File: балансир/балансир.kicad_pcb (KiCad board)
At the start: 2 copper layers, 0 parts

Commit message: добавлена STM32
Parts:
- added C1: 4.7мкФ, 1210, N_RLC:Конденсатор_SMD_1210, F.Cu at (233.8, 99.5)
- added C10: 4.7мкФ, 1210, N_RLC:Конденсатор_SMD_1210, F.Cu at (227.5, 100.9)
- added C11: 4.7мкФ, 1210, N_RLC:Конденсатор_SMD_1210, F.Cu at (227.4, 96.6)
- added C12: 4.7мкФ, 1210, N_RLC:Конденсатор_SMD_1210, F.Cu at (249.5, 82.7)
- added C13: 4.7мкФ, 1210, N_RLC:Конденсатор_SMD_1210, F.Cu at (255.8, 77.1)
- added C14: 4.7мкФ, 1210, N_RLC:Конденсатор_SMD_1210, F.Cu at (227.5, 105.2)
- added C15: 4.7мкФ, 1210, N_RLC:Конденсатор_SMD_1210, F.Cu at (245.0, 87.0)
- added C16: 4.7мкФ, 1210, N_RLC:Конденсатор_SMD_1210, F.Cu at (232.4, 90.9)
- added C17: 4.7мкФ, 1210, N_RLC:Конденсатор_SMD_1210, F.Cu at (240.0, 95.2)
- added C2: 4.7мкФ, 1210, N_RLC:Конденсатор_SMD_1210, F.Cu at (243.2, 78.4)
- added C3: 4.7мкФ, 1210, N_RLC:Конденсатор_SMD_1210, F.Cu at (251.9, 72.8)
- added C4: 4.7мкФ, 1210, N_RLC:Конденсатор_SMD_1210, F.Cu at (221.2, 104.6)
- added C5: 4.7мкФ, 1210, N_RLC:Конденсатор_SMD_1210, F.Cu at (243.2, 82.7)
- added C6: 4.7мкФ, 1210, N_RLC:Конденсатор_SMD_1210, F.Cu at (249.5, 78.4)
- added C7: 4.7мкФ, 1210, N_RLC:Конденсатор_SMD_1210, F.Cu at (238.7, 90.9)
- added C8: 4.7мкФ, 1210, N_RLC:Конденсатор_SMD_1210, F.Cu at (233.7, 95.2)
- added C9: 4.7мкФ, 1210, N_RLC:Конденсатор_SMD_1210, F.Cu at (258.2, 72.8)
- added DA1: МОП-реле_КР293КП4, MOTOR_DD:DIP8, F.Cu at (199.9, 73.3)
- added DA2: МОП-реле_КР293КП4, MOTOR_DD:DIP8, F.Cu at (199.9, 86.4)
- added DD1: ATmega8A-AU, N_DD:микросхема_ATMEGA-8-161AU, F.Cu at (193.8, 114.0)
- added DD2: 5559ИН10_28(UART-RS485), N_DD:SO-8, F.Cu at (223.1, 98.0)
- added G1: стабилизатор_нерегулируемый_LM2931, N_G:Стабилизатор_корпус_TO-92, F.Cu at (231.9, 87.1)
- added R1: Резистор_0,125Вт, N_RLC:Резистор_SMD_0805_0,125Вт, F.Cu at (232.5, 77.1)
- added R10: Резистор_0,125Вт, N_RLC:Резистор_SMD_0805_0,125Вт, F.Cu at (239.7, 98.6)
- added R11: Резистор_0,125Вт, N_RLC:Резистор_SMD_0805_0,125Вт, F.Cu at (245.9, 93.1)
- added R12: Резистор_0,125Вт, N_RLC:Резистор_SMD_0805_0,125Вт, F.Cu at (251.0, 88.8)
- added R13: 20к, 0805, N_RLC:Резистор_SMD_0805_0,125Вт, F.Cu at (233.4, 105.5)
- added R14: Резистор_0,125Вт, N_RLC:Резистор_SMD_0805_0,125Вт, F.Cu at (259.6, 80.6)
- added R15: Резистор_0,125Вт, N_RLC:Резистор_SMD_0805_0,125Вт, F.Cu at (255.5, 83.2)
- added R16: Резистор_0,125Вт, N_RLC:Резистор_SMD_0805_0,125Вт, F.Cu at (237.5, 102.9)
- added R17: Резистор_0,125Вт, N_RLC:Резистор_SMD_0805_0,125Вт, F.Cu at (255.1, 86.2)
- added R2: Резистор_0,125Вт, N_RLC:Резистор_SMD_0805_0,125Вт, F.Cu at (210.5, 106.3)
- added R3: Резистор_0,125Вт, N_RLC:Резистор_SMD_0805_0,125Вт, F.Cu at (236.6, 77.1)
- added R4: Резистор_0,125Вт, N_RLC:Резистор_SMD_0805_0,125Вт, F.Cu at (214.6, 106.3)
- added R5: Резистор_0,125Вт, N_RLC:Резистор_SMD_0805_0,125Вт, F.Cu at (238.8, 85.8)
- added R6: Резистор_0,125Вт, N_RLC:Резистор_SMD_0805_0,125Вт, F.Cu at (244.7, 90.5)
- added R7: Резистор_0,125Вт, N_RLC:Резистор_SMD_0805_0,125Вт, F.Cu at (255.5, 80.6)
- added R8: Резистор_0,125Вт, N_RLC:Резистор_SMD_0805_0,125Вт, F.Cu at (233.4, 102.9)
- added R9: Резистор_0,125Вт, N_RLC:Резистор_SMD_0805_0,125Вт, F.Cu at (251.0, 86.2)
- added VD1: Диод_шоттки(2-анод), N_VD_HL:Диод_BAR43CFILM_SOT-23, F.Cu at (244.5, 99.1)
- added VD10: Диод_шоттки(2-анод), N_VD_HL:Диод_BAR43CFILM_SOT-23, F.Cu at (260.2, 83.6)
- added VD2: Диод_шоттки(2-анод), N_VD_HL:Диод_BAR43CFILM_SOT-23, F.Cu at (255.7, 89.2)
- added VD3: Диод_шоттки(2-анод), N_VD_HL:Диод_BAR43CFILM_SOT-23, F.Cu at (242.3, 102.6)
- added VD4: Диод_шоттки(2-анод), N_VD_HL:Диод_BAR43CFILM_SOT-23, F.Cu at (250.7, 95.4)
- added VD5: Диод_шоттки(2-анод), N_VD_HL:Диод_BAR43CFILM_SOT-23, F.Cu at (247.9, 98.9)
- added VD6: Диод_шоттки(2-анод), N_VD_HL:Диод_BAR43CFILM_SOT-23, F.Cu at (259.8, 87.2)
- added VD7: Диод_шоттки(2-анод), N_VD_HL:Диод_BAR43CFILM_SOT-23, F.Cu at (254.1, 92.8)
- added VD8: Диод_шоттки(2-анод), N_VD_HL:Диод_BAR43CFILM_SOT-23, F.Cu at (250.7, 91.8)
- added VD9: Диод_шоттки(2-анод), N_VD_HL:Диод_BAR43CFILM_SOT-23, F.Cu at (245.7, 102.6)
- added VT1: Транзистор_полевой_P-канал, N_VD_HL:Транзистор_P_IRF9Z24NPBF, F.Cu at (105.5, 87.2)
- added VT2: Транзистор_полевой_P-канал, N_VD_HL:Транзистор_P_IRF9Z24NPBF, F.Cu at (123.0, 87.2)
- added VT3: Транзистор_полевой_P-канал, N_VD_HL:Транзистор_P_IRF9Z24NPBF, F.Cu at (112.8, 62.2)
- added VT4: Транзистор_полевой_P-канал, N_VD_HL:Транзистор_P_IRF9Z24NPBF, F.Cu at (127.0, 63.0)
- added VT5: Транзистор_полевой_P-канал, N_VD_HL:Транзистор_P_IRF9Z24NPBF, F.Cu at (108.4, 143.9)
- added VT6: Транзистор_полевой_P-канал, N_VD_HL:Транзистор_P_IRF9Z24NPBF, F.Cu at (108.4, 149.1)
- added VT7: Транзистор_полевой_N-канал, N_VD_HL:Транзистор_N_STP10NK60Z, F.Cu at (119.2, 143.3)
- added VT8: Транзистор_полевой_N-канал, N_VD_HL:Транзистор_N_STP10NK60Z, F.Cu at (119.2, 148.1)
- added X1: Клеммник_х2, N_X:Клеммник_х2_шаг5, F.Cu at (187.5, 53.5)
- added X2: Клеммник_х2, N_X:Клеммник_х2_шаг5, F.Cu at (202.5, 51.2)
- added X3: Клеммник_х2, N_X:Клеммник_х2_шаг5, F.Cu at (201.4, 101.4)
- added X5: Средняя точка(M12), N_X:Отверстие_М12, F.Cu at (75.0, 84.5)
- added X6: Минус(M12), N_X:Отверстие_М12, F.Cu at (155.0, 84.5)
- added XP1: Вилка_PLD6_ПРОГ, N_X:Вилка_PLD6_вертикальная, F.Cu at (243.8, 74.7)
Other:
- board outline added: 80 x 60 mm

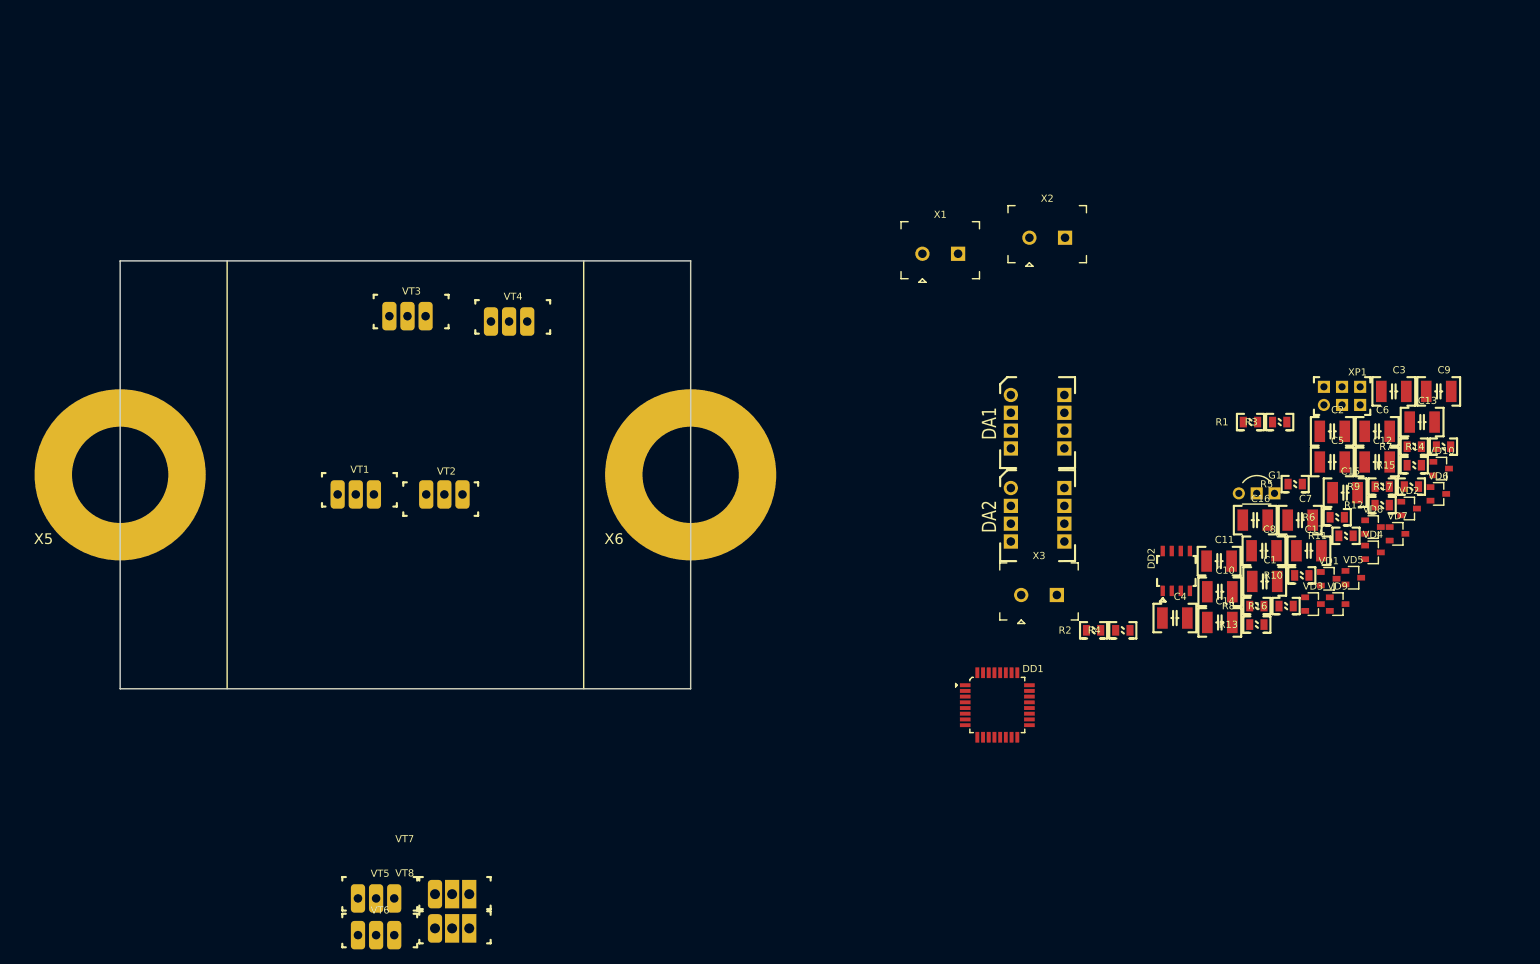
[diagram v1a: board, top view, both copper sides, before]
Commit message: atmega8 заменена на stm32 разводка не готова
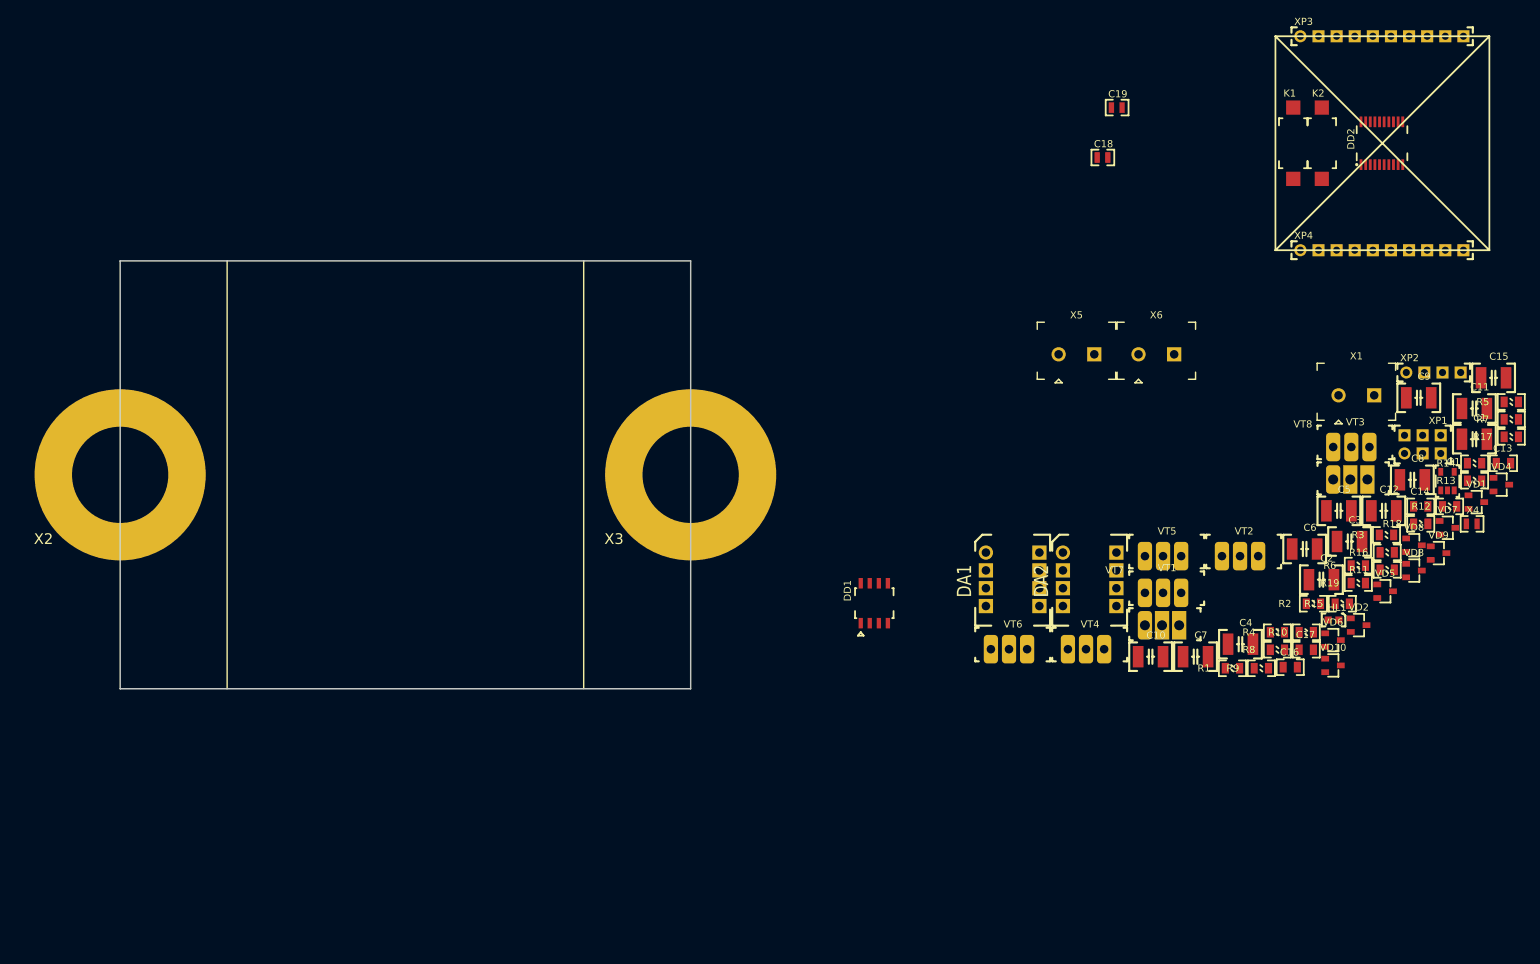
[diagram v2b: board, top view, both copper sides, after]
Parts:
- removed the X2 at (202.5, 51.2)
- removed the X3 at (201.4, 101.4)
- added C18: 12Ф, 0603, N_RLC:Конденсатор_SMD_0603, F.Cu at (212.0, 40.0)
- added C19: 12Ф, 0603, N_RLC:Конденсатор_SMD_0603, F.Cu at (214.0, 33.0)
- added HL1: Светодиод, N_VD_HL:Светодиод_SMD_0603, F.Cu at (244.4, 104.9)
- added K1: 1437566-3 (FSMSM), N_X:Кнопка_FSMSM, F.Cu at (239.5, 43.0)
- added K2: 1437566-3 (FSMSM), N_X:Кнопка_FSMSM, F.Cu at (243.5, 43.0)
- added R18: Резистор_0,125Вт, N_RLC:Резистор_SMD_0805_0,125Вт, F.Cu at (256.4, 91.4)
- added R19: Резистор_0,125Вт, N_RLC:Резистор_SMD_0805_0,125Вт, F.Cu at (247.6, 99.7)
- added X4: перемычка_разрывная, N_RLC:Конденсатор_SMD_0603, F.Cu at (263.8, 91.4)
- added X5: Клеммник_х2, N_X:Клеммник_х2_шаг5, F.Cu at (206.6, 67.6)
- added X6: Клеммник_х2, N_X:Клеммник_х2_шаг5, F.Cu at (217.8, 67.6)
- added XP2: Вилка_PLS4, N_X:Вилка_PLS4_вертикальная, F.Cu at (255.4, 70.2)
- added XP3: Вилка_PLS10, N_X:Вилка_PLS10_вертикальная, F.Cu at (240.5, 23.0)
- added XP4: Вилка_PLS10, N_X:Вилка_PLS10_вертикальная, F.Cu at (240.5, 53.0)
- C13, C14, C16, C17: value 4.7мкФ, 1210 -> 4.7мкФ, 0805; footprint N_RLC:Конденсатор_SMD_1210 -> N_RLC:Конденсатор_SMD_0805
- DD1: value ATmega8A-AU -> 5559ИН10_28(UART-RS485); footprint N_DD:микросхема_ATMEGA-8-161AU -> N_DD:SO-8
- DD2: value 5559ИН10_28(UART-RS485) -> STM32F030F4P6(TSSOP-20); footprint N_DD:SO-8 -> N_DD:SSOP-20
- G1: value стабилизатор_нерегулируемый_LM2931 -> стабилизатор_нерегулируемый_MC78LC33NTRG; footprint N_G:Стабилизатор_корпус_TO-92 -> N_G:Преобразователь_LM2703_SOT-23-5
- R16: value Резистор_0,125Вт -> 20к, 0805
- moved VT8 140.8 mm to (245.1, 85.2)
- moved VT3 133.6 mm to (245.1, 80.6)
- moved VT5 120.3 mm to (218.7, 95.9)
- moved VT1 114.0 mm to (218.7, 101.1)
- moved VT2 106.9 mm to (229.5, 95.9), turned to 0 degrees
- moved VT7 106.4 mm to (218.7, 105.6)
- moved VT6 97.4 mm to (197.1, 109.0)
- moved VT4 93.0 mm to (207.9, 109.0)
- moved DD2 62.6 mm to (249.0, 41.0), turned to 90 degrees
- moved X1 61.6 mm to (245.9, 73.4)
- moved C11 41.7 mm to (263.2, 75.2)
- moved R13 36.6 mm to (263.9, 85.3)
- moved C1 35.5 mm to (263.2, 79.5)
- moved R1 34.6 mm to (230.0, 111.6)
- moved C14 33.2 mm to (256.4, 88.9)
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- renumbered X5 to X2, X6 to X3
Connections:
- C13 pad 1: /+5 -> /+3В
- C13 pad 2: /GND -> /ADC_T1
- C14 pad 1: Net-(C14-Pad1) -> /ADCT2
- C15 pad 1: /VCC -> /+5В_эфир
- C15 pad 2: /0В -> /GND_эфир
- DA1 pad 4: /GND -> /GND_эфир
- DD1 pad 1: Net-(DD1-Pad1) -> /RX_ext
- DD1 pad 2: Net-(DD1-Pad2) -> /EnRS_ext
- DD1 pad 3: /0В -> /EnRS_ext
- DD1 pad 4: /VCC -> /TX_ext
- DD1 pad 5: /0В -> /GND_эфир
- DD1 pad 6: /VCC -> /A
- DD1 pad 7: Net-(DD1-Pad7) -> /B
- DD1 pad 8: Net-(DD1-Pad8) -> /+5В_эфир
- DD2 pad 1: /RX_ext -> /BOOT_mode
- DD2 pad 2: /EnRS_ext -> /G4
- DD2 pad 3: /EnRS_ext -> /G3
- DD2 pad 4: /TX_ext -> /RES
- DD2 pad 5: /GND -> /VCC
- DD2 pad 6: /A -> /G2
- DD2 pad 7: /B -> /G1
- DD2 pad 8: /+5 -> /TX
- G1 pad 1: /+5В -> /0В
- G1 pad 2: /0В -> /+6В
- G1 pad 3: /+6В -> /VCC
- R13 pad 1: /VCC -> /0В
- R13 pad 2: /RES -> /BOOT_mode
- R14 pad 2: /GND -> /GND_эфир
- R15 pad 2: /GND -> /GND_эфир
- R16 pad 1: /RX_ext -> /VCC
- R16 pad 2: /GND -> /RES
- R4 pad 2: /ADC5 -> /ADC5_6V
- R5 pad 2: /ADC6 -> /ADC_3V
- R6 pad 2: /ADC1 -> /ADCT2
- R7 pad 1: /ADC5 -> /ADC5_6V
- R8 pad 1: /ADC6 -> /ADC_3V
- R9 pad 1: /ADC0 -> /ADC_T1
- VD7 pad 2: /+5В -> /+3В
- XP1 pad 1: /MISO -> /DIO
- XP1 pad 3: /SCK -> /CLK
- XP1 pad 4: /MOSI -> /BOOT_mode
